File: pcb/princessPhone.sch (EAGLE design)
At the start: 8 parts, among them Q1 BF245, U1 AG1170-S3

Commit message: Added power, audio, usb.
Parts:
- added C10, C28: 0.1UF, rcl:C-USC0402
- added C26: 1UF, rcl:C-USC0402
- added C27: 10UF, rcl:C-USC0603
- added C5, C6: (no value), rcl:C-USC0603
- added IC1: OPA2134UA, linear:OPA2134UA
- added LED1: BLUE, led:LEDCHIPLED_0603
- added LED2: RED, led:LEDCHIPLED_0603
- added P2: TC2030-MCP-NL, raveGearControl:TC2030-MCP-NL
- added R10, R19, R20, R21: 0, rcl:R-US_R0603
- added R11: 47K, rcl:R-US_R0603
- added R12: 22K, rcl:R-US_R0603
- added R13, R14, R15, R16, R17, R18, R7: 47, rcl:R-US_R0603
- added R3, R6, R8: 10K, rcl:R-US_R0402
- added R4, R5: (no value), rcl:R-US_R0603
- added R9: 470, rcl:R-US_R0603
- added TP13, TP14: PTR1B1,27, testpad:PTR1B1,27
- added TP15, TP16, TP17, TP18: PTR1B2,54, testpad:PTR1B2,54
- added U2: PIC32MX170D, raveGear5:PIC32MX170D
- added U3: BLUETOOTH-RN-52, SparkFun-RF:BLUETOOTH-RN-52
- added U4: V_REG_LD1085D2, SparkFun-PowerIC:V_REG_LD1085D2
- added X1: 22-23-2041, con-molex:22-23-2041
- added X3: USB_MICRO_B, FosBattery1:USB_MICRO_B
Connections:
- removed net F/R: U1.F/R
- removed net PD: R2.2
- removed net RM: U1.RM
- removed net SHK: U1.SHK
- new net +2V5: P2.LVP
- new net AG1170_F/R: U1.F/R, U2PORTC.RPC4/PMA4/RC4
- new net AG1170_PD: R2.2, U2PORTC.RPC6/PMA1/RC6
- new net AG1170_RM: U1.RM, U2PORTC.RPC3/RC3
- new net AG1170_SHK: U1.SHK, U2PORTC.RPC5/PMA3/RC5
- new net FPGA_SPI_SS: U2PORTB.RPB7/CTED3/PMD5/INT0/RB7
- new net MCLR#: P2.VPP/MCLR, R3.1, U2PWR.#MCLR
- new net N$10: LED2.C, R9.2
- new net N$12: IC1B.OUT, R16.2, R17.2, R18.1
- new net N$4: C27.1, U2PWR.VCAP
- new net N$5: R7.1, U3.LED0
- new net N$6: X1-4.S
- new net N$7: R9.1, U3.LED1
- new net N$8: R4.1, R5.2, U4.ADJ
- new net N$9: LED1.C, R7.2
- new net PIC32_MISO: U2PORTB.RPB8/SCL1/CTED10/PMD4/RB8
- new net PIC32_MOSI: U2PORTB.PGED3/RPB5/PMD7/RB5
- new net PIC32_PGEC1: P2.ICSP_CLK/PGC, U2PORTB.PGEC1/AN3/C1INC/C2INA/RPB1/CTED12/RB1
- new net PIC32_PGED1: P2.ICSP_DAT/PGD, U2PORTB.PGED1/AN2/C1IND/C2INB/C3IND/RPB0/RB0
- new net PIC32_SCK: U2PORTB.CVREFOUT/AN10/C3INB/RPB14/SCK1/CTED5/PMWR/RB14
- new net PIC32_SCL2: R8.1, TP14.TP, U2PORTB.AN5/C1INA/C2INC/RTCC/RPB3/SCL2/RB3
- new net PIC32_SDA2: R6.1, TP13.TP, U2PORTB.AN4/C1INB/C2IND/RPB2/SDA2/CTED13/RB2
- new net PIC32_U1CTS#_3V3: U2PORTA.VREF-/CVREF-/AN1/RPA1/CTED2/RA1, U3.UART_RTS
- new net PIC32_U1RTS#_3V3: U2PORTB.PGED2/RPB10/CTED11/PMD2/RB10, U3.UART_CTS
- new net PIC32_U1RX_3V3: U2PORTC.AN7/RPC1/RC1, U3.UART_TX
- new net PIC32_U1TX_3V3: U2PORTC.AN6/RPC0/RC0, U3.UART_RX
- new net RING: U1.RING(B), X1-1.S
- new net RN52_CMD_MODE#: U2PORTC.RPC9/CTED7/PMA6/RC9, U3.GPIO9
- new net RN52_DFU_MODE: R11.2, R12.2, U3.GPIO3
- new net RN52_EVENT#: U2PORTC.RPC8/PMA5/RC8, U3.GPIO2
- new net RN52_FACTORY_RST: U3.GPIO4
- new net RN52_MIC_L+: R16.1, U3.MIC_L+
- new net RN52_MIC_L-: R21.1, U3.MIC_L-
- new net RN52_MIC_R+: R17.1, U3.MIC_R+
- new net RN52_MIC_R-: R20.1, U3.MIC_R-
- new net RN52_PWREN: U2PORTC.RPC7/PMA0/RC7, U3.PWREN
- new net RN52_SPKR_L+: R13.1, U3.SPKR_L+
- new net RN52_SPKR_L-: R10.1, U3.SPKR_L-
- new net RN52_SPKR_R+: R14.1, U3.SPKR_R+
- new net RN52_SPKR_R-: R19.1, U3.SPKR_R-
- new net RN52_SPKR_SUM: IC1A.+IN, R13.2, R14.2, R15.1
- new net ROTARY: X1-3.S
- new net SST25_CE#: U2PORTB.AN12/PMD0/RB12
- new net SST25_MISO: U2PORTC.AN8/RPC2/PMA2/RC2
- new net SST25_MOSI: U2PORTB.AN11/RPB13/CTPLS/PMRD/RB13
- new net SST25_SCK: U2PORTB.AN9/C3INA/RPB15/SCK2/CTED6/PMCS1/RB15
- new net TIP: U1.TIP(A), X1-2.S
- new net USB_DM: TP16.TP, U3.USBD-, X3.2
- new net USB_DP: TP17.TP, U3.USBD+, X3.3
- new net USB_VBUS: C5.1, R12.1, TP15.TP, U4.IN, X3.1
- new net VCC: P2.VDD
- net +3V3: now also C10.1, C26.1, C28.1, C6.1, IC1A.V+, LED1.A, LED2.A, R3.2, R4.2, R6.2, R8.2, U2PWR.AVDD, U2PWR.VDD@1, U2PWR.VDD@2, U3.VDD, U4.OUT, U4.OUT@1
- net AG1170_AUDIO_IN: now also IC1A.OUT, R15.2
- net AG1170_AUDIO_OUT: now also IC1B.+IN, R18.2
- net GND: now also C10.2, C26.2, C27.2, C28.2, C5.2, C6.2, IC1A.-IN, IC1A.V-, IC1B.-IN, P2.VSS(GND), R10.2, R11.1, R19.2, R20.2, R21.2, R5.1, TP18.TP, U2PWR.AVSS, U2PWR.PAD, U2PWR.VSS@1, U2PWR.VSS@2, U2PWR.VSS@3, U3.AGND, U3.GND, U3.GND1, U3.GND2, U3.GND3, U3.GND4, U3.GND5, U3.GND6, U3.GND7, U3.GND8, U3.GND9, X3.5
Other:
- note added: "*ERRATA ON RA(0,1)"
- note added: "*ERRATUM ON RA3"
- note added: "1. 5V TOLERANT GPIO: MCLR RA7, RA8, RA9, RA10 RB5, RB6, RB7, RB8, RB9,RB10, RB11, RB12 RC4, RC5, RC6, RC7, RC8, RC9"
- note added: "2015.07.12"
- note added: "ADDED POWER SUPPORT, AUDIO AMPS, USB,"
- note added: "AUTHOR"
- note added: "MCU NOTES:"
- note added: "TODO: DOES SHK TOGGLE DURING DIALER ROTATION?"
- note removed: "AYTHOR"

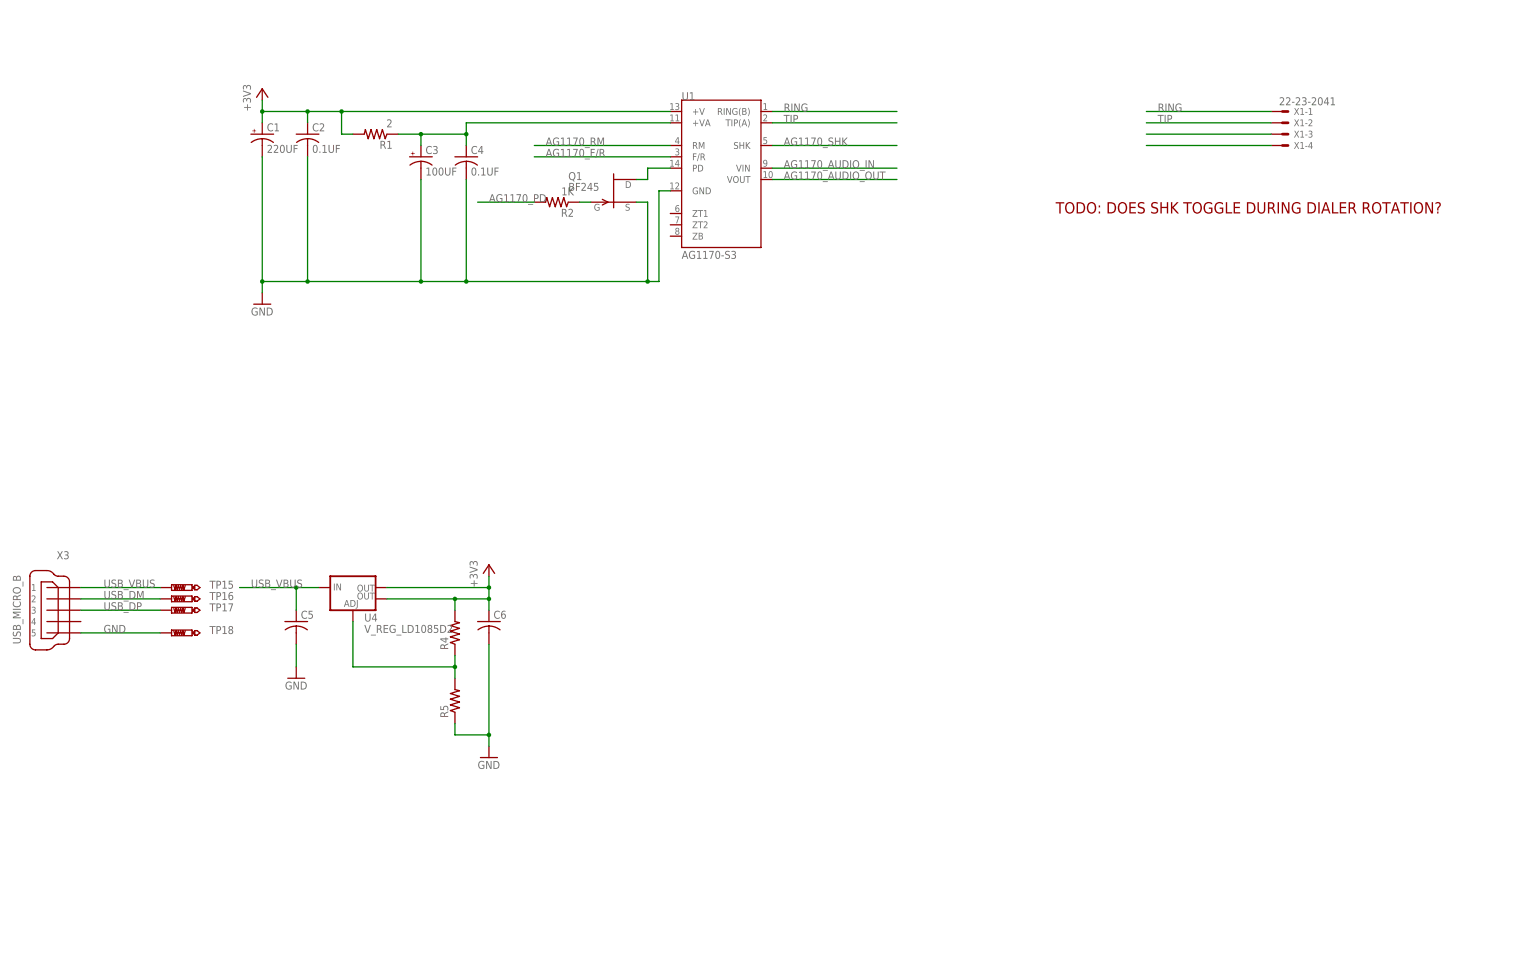
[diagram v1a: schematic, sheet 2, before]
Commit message: -Changed MCU package -Added RJ-11 connector
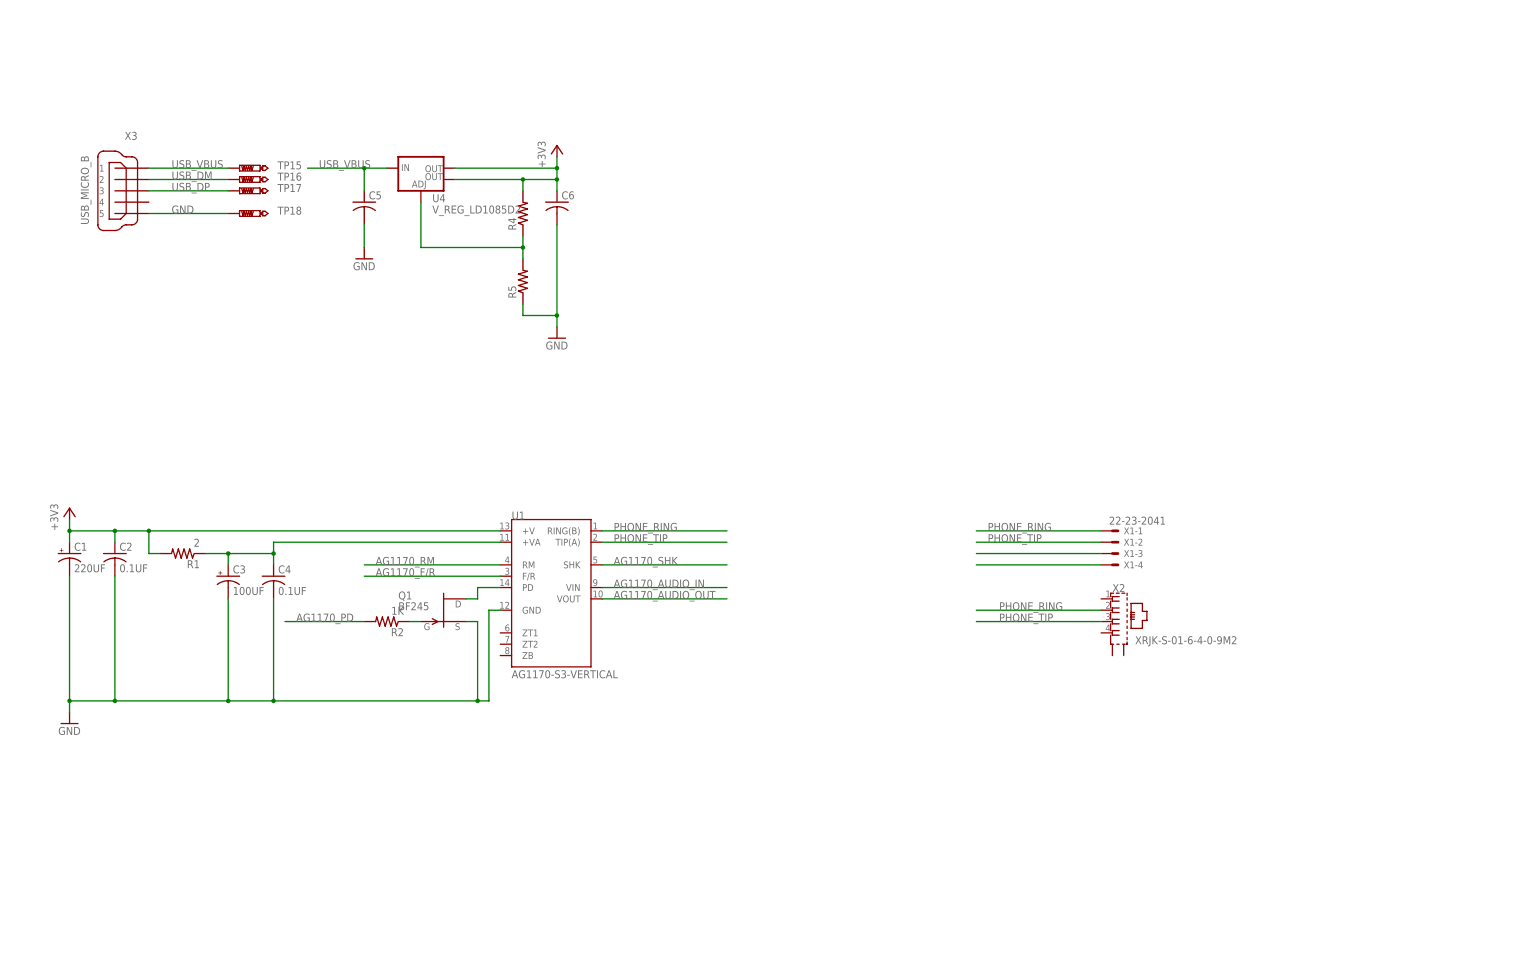
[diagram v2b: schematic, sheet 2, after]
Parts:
- added X2: XRJK-S-01-6-4-0-9M2, con-xmultiple:XRJK-S-01-6-4-0-9M2
- U1: value AG1170-S3 -> AG1170-S3-VERTICAL; device princessPhone:AG1170-S3 -> princessPhone:AG1170-S3-VERTICAL
- U2: value PIC32MX170D -> PI32MX170D-PT; device raveGear5:PIC32MX170D -> raveGear5:PI32MX170D-PT
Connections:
- removed net +2V5: P2.LVP
- removed net RING: U1.RING(B), X1-1.S
- removed net TIP: U1.TIP(A), X1-2.S
- new net PHONE_RING: U1.RING(B), X1-1.S, X2.2
- new net PHONE_TIP: U1.TIP(A), X1-2.S, X2.3
- net GND: no longer U2PWR.PAD
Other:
- note added: "2015.07.17"
- note added: "CHANGED MCU PACKAGE, ADDED RJ-11 CONNECTOR"
- note removed: "TODO: DOES SHK TOGGLE DURING DIALER ROTATION?"
- moved on the sheet: C1, C2, C3, C4, C5, C6, Q1, R1, R2, R4, R5, TP15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

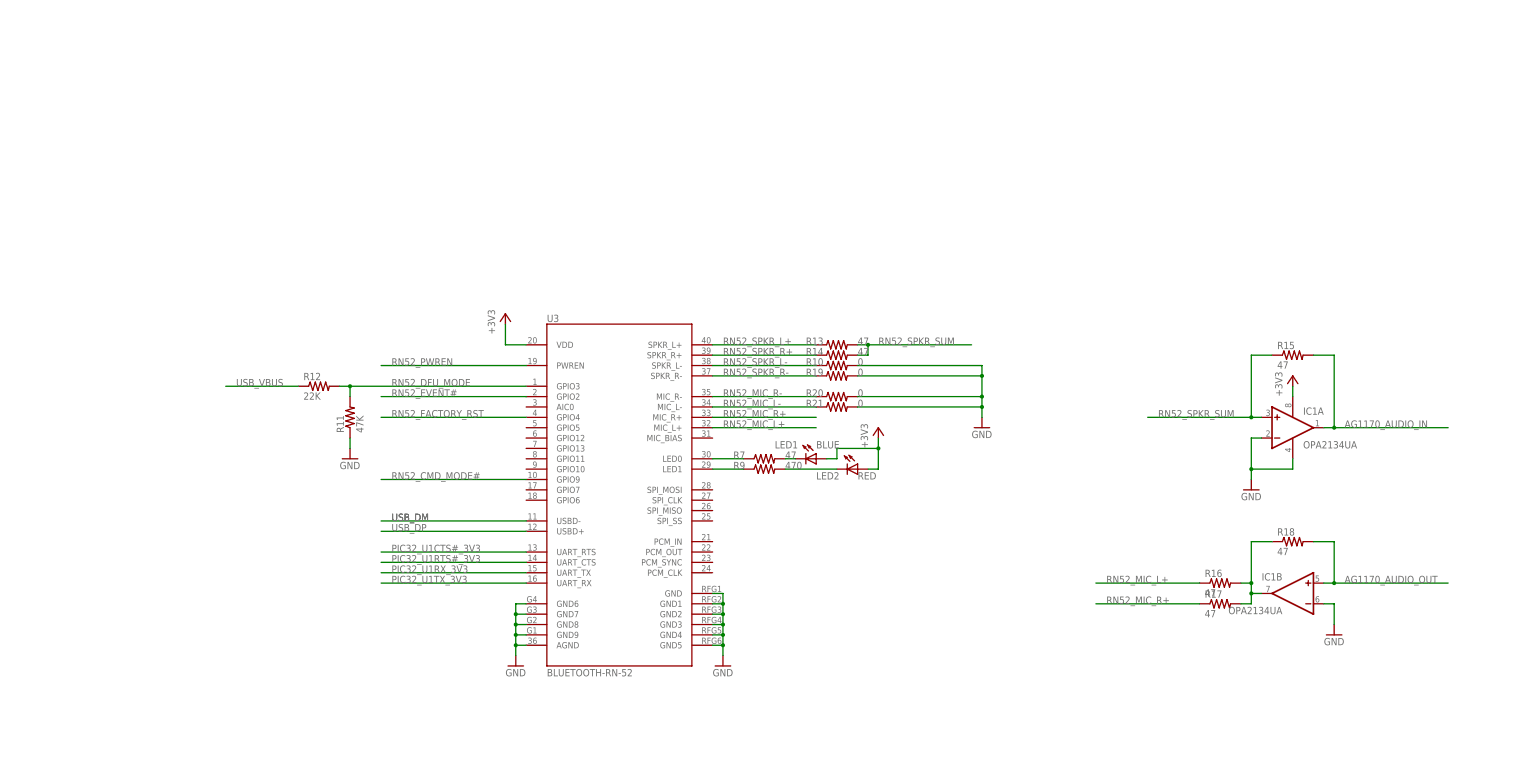
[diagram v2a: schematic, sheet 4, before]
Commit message: -Added to library -Added line-level components -Cleaned up schematic
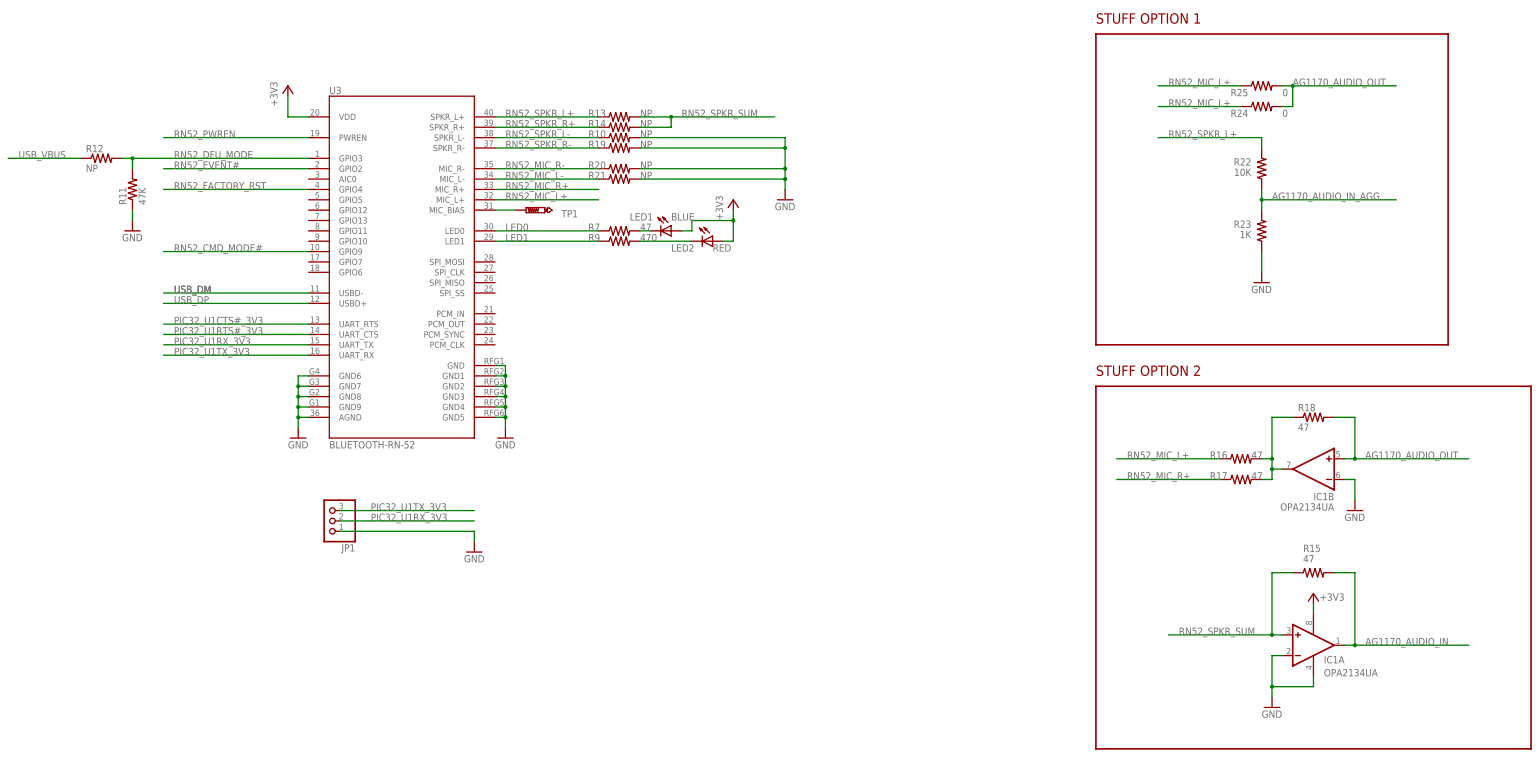
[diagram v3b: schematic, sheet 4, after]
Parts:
- removed TP15, TP16, TP17, TP18: PTR1B2,54, testpad:PTR1B2,54
- added JP1: (no value), pinhead:PINHD-1X3
- added R22, R26, R27, R28, R29: 10K, rcl:R-US_R0603
- added R23: 1K, rcl:R-US_R0603
- added R24, R25: 0, rcl:R-US_R0603
- added SW3, SW4, SW5, SW6: LL1105BF250Q, raveGearControl:LL1105BF250Q
- added TP1, TP10, TP11, TP12, TP19, TP2, TP20, TP21, TP22, TP23, TP3, TP4, TP5, TP6, TP7, TP8, TP9: PTR1B1,27, testpad:PTR1B1,27
- Q1: value BF245 -> 2N7002K; device transistor-fet:BF245 -> princessPhone:2N7002K
- R10, R19, R20, R21: value 0 -> NP
- R12: value 22K -> NP
- R13, R14: value 47 -> NP
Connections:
- net N$5 renamed LED0
- net N$7 renamed LED1
- removed net FPGA_SPI_SS: U2PORTB.RPB7/CTED3/PMD5/INT0/RB7
- removed net N$6: X1-4.S
- removed net PIC32_MISO: U2PORTB.RPB8/SCL1/CTED10/PMD4/RB8
- removed net PIC32_MOSI: U2PORTB.PGED3/RPB5/PMD7/RB5
- removed net PIC32_SCK: U2PORTB.CVREFOUT/AN10/C3INB/RPB14/SCK1/CTED5/PMWR/RB14
- removed net ROTARY: X1-3.S
- removed net VCC: P2.VDD
- new net AG1170_AUDIO_IN_AGG: R22.1, R23.2
- new net N$11: TP1.TP, U3.MIC_BIAS
- new net PIC32_RSVD_1: TP6.TP, U2PORTA.VREF+/CVREF+/AN0/C3INC/RPA0/CTED1/RA0
- new net PIC32_RSVD_10: TP3.TP, U2PORTB.RPB9/SDA1/CTED4/PMD3/RB9
- new net PIC32_RSVD_11: TP4.TP, U2PORTB.PGEC2/RPB11/PMD1/RB11
- new net PIC32_RSVD_12: TP5.TP, U2PORTB.CVREFOUT/AN10/C3INB/RPB14/SCK1/CTED5/PMWR/RB14
- new net PIC32_RSVD_2: TP7.TP, U2PORTA.OSC1/CLKI/RPA2/RA2
- new net PIC32_RSVD_3: TP8.TP, U2PORTA.OSC2/CLKO/RPA3/RA3
- new net PIC32_RSVD_4: TP9.TP, U2PORTA.SOSCO/RPA4/T1CK/CTED9/RA4
- new net PIC32_RSVD_5: TP10.TP, U2PORTA.PGEC/TCK/CTED8/PMA7/RA7
- new net PIC32_RSVD_6: TP11.TP, U2PORTA.TDO/RPA8/PMA8/RA8
- new net PIC32_RSVD_7: TP12.TP, U2PORTA.TDI/RPA9/PMA9/RA9
- new net PIC32_RSVD_8: TP19.TP, U2PORTA.PGED/TMS/PMA10/RA10
- new net PIC32_RSVD_9: TP2.TP, U2PORTB.SOSCI/RPB4/RB4
- new net SW0: R26.2, SW3.S, U2PORTB.PGED3/RPB5/PMD7/RB5
- new net SW1: R27.2, SW4.S, U2PORTB.PGEC3/RPB6/PMD6/RB6
- new net SW2: R28.2, SW5.S, U2PORTB.RPB7/CTED3/PMD5/INT0/RB7
- new net SW3: R29.2, SW6.S, U2PORTB.RPB8/SCL1/CTED10/PMD4/RB8
- net +3V3: now also P2.VDD, R26.1, R27.1, R28.1, R29.1
- net AG1170_AUDIO_OUT: now also R24.2, R25.2
- net GND: now also JP1.1, R23.1, SW3.P, SW4.P, SW5.P, SW6.P; no longer TP18.TP
- net PIC32_U1RX_3V3: now also JP1.2
- net PIC32_U1TX_3V3: now also JP1.3
- net RN52_MIC_L+: now also R24.1, R25.1
- net RN52_SPKR_L+: now also R22.2
- net SST25_CE#: now also TP20.TP
- net SST25_MISO: now also TP23.TP
- net SST25_MOSI: now also TP21.TP
- net SST25_SCK: now also TP22.TP
- net USB_DM: no longer TP16.TP
- net USB_DP: no longer TP17.TP
- net USB_VBUS: no longer TP15.TP
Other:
- note added: "STUFF OPTION 1"
- note added: "STUFF OPTION 2"
- moved on the sheet: IC1A, IC1B, LED1, LED2, R10, R11, R12, R13, R14, R15, R16, R17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
